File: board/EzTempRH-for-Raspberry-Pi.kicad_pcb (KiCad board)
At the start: 2 copper layers, 30 x 15 mm, 19 parts, among them P1 CONN_4, P2 CONN_4, P3 CONN_5, U1 CY8C4100-28SSOP, U2 HIH5030

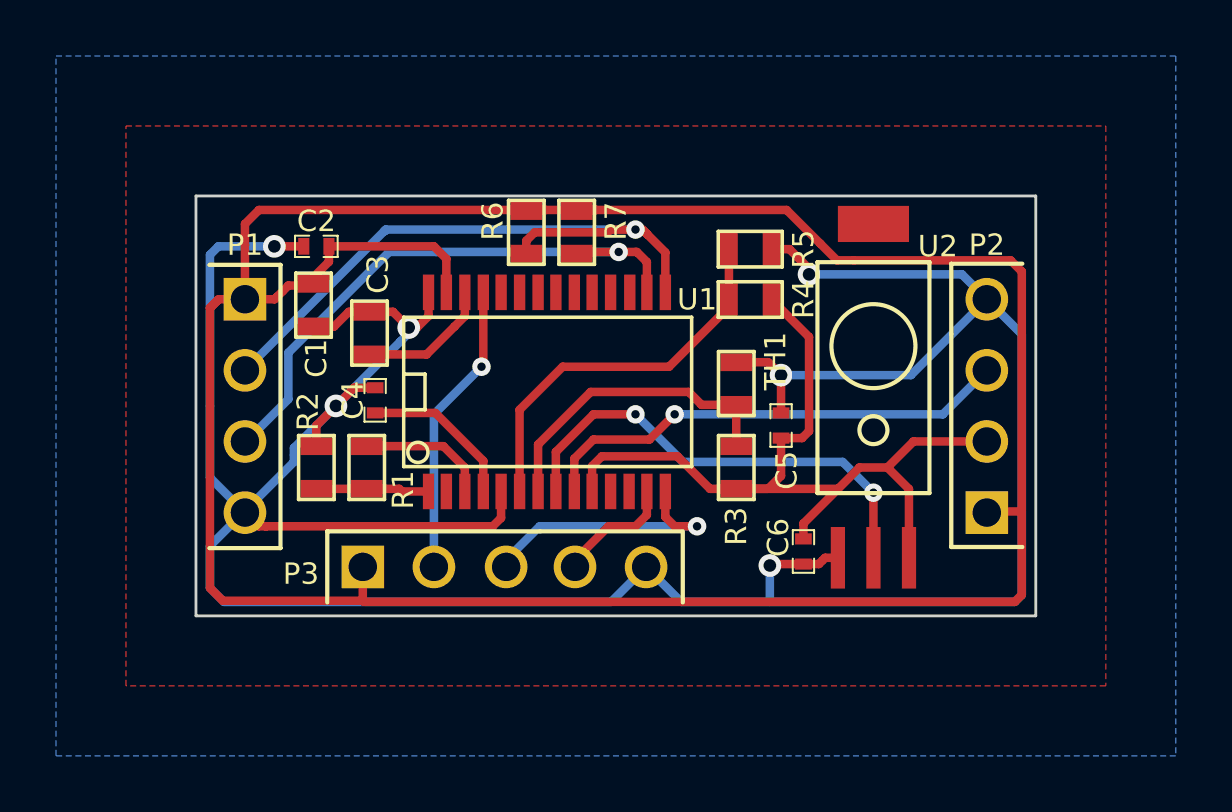
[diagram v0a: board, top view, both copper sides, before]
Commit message: Silkscreen text and programming fix
Added silkscreen text on pins.
Fix a minor issue with the programming connector and pins position.
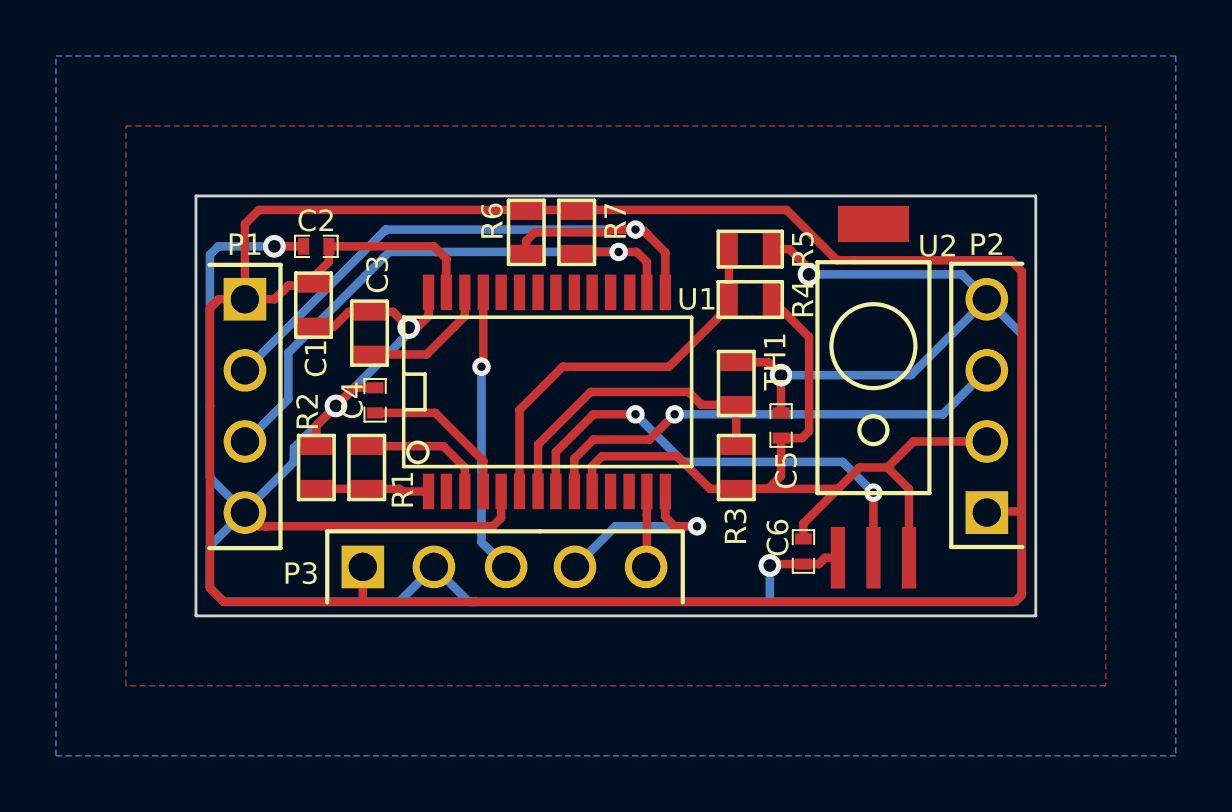
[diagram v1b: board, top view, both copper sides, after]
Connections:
- P3 pad 2: /XRES -> /Vss
- P3 pad 3: /SWDCK -> /XRES
- P3 pad 4: /SWDIO -> /SWDCK
- P3 pad 5: /Vss -> /SWDIO
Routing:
- net /Vss: track 110.7 -> 113.4 mm
- net /SWDCK: track 9.50 -> 7.14 mm
- net /SWDIO: track 4.07 -> 2.71 mm
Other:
- board text added: "3.3V"
- board text added: "EN"
- board text added: "EXT"
- board text added: "EzTemp&RH rev1.0"
- board text added: "GND"
- board text added: "RX"
- board text added: "TX"

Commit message: DFM correction
Corrected R6 and R7 for manufacturing
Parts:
- moved R7 1.36 mm to (40.5, 31.7), turned to 180 degrees
- moved R6 0.50 mm to (43.3, 31.7), turned to 0 degrees
- moved U2 0.10 mm to (54.2, 36.1)
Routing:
- net /Vddd: track 98.0 -> 111.0 mm, vias 0 -> 2
- net /RX: track 23.6 -> 21.3 mm, vias 1 -> 2
- net /RH_T: track 16.8 -> 18.2 mm
- net /EN: track 31.7 -> 33.1 mm
- net /TX: track 20.9 -> 22.1 mm
